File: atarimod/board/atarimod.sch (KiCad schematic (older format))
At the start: 14 parts, among them IC1 74HC14D, IC2 74HC14D, IC3 74HC14D, IC4 74HC14D, P1 CONN_02X20, P2 CONN_02X10, U2 APE8865N-33-HF-3

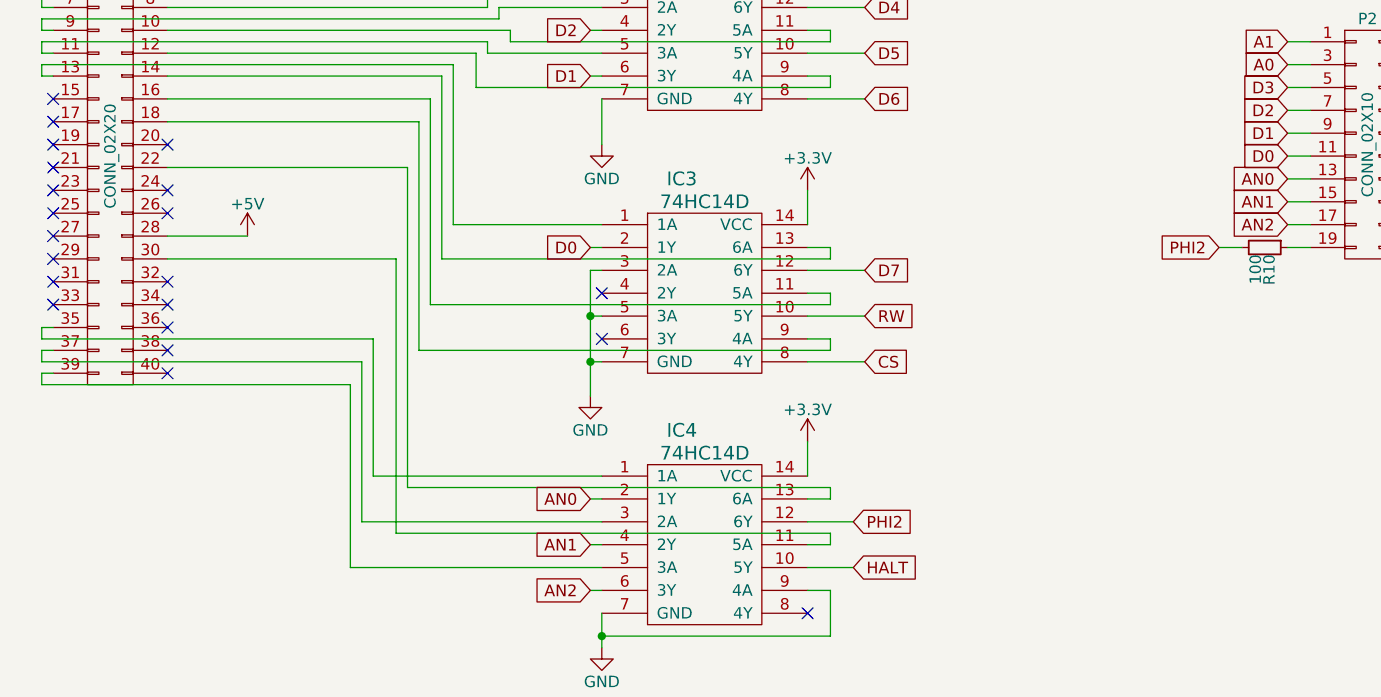
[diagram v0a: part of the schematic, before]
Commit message: Fixed a bug in the board layout
Working version now on Atari 800XL.
But in the mod board that needed some botching. Fixed in schematic and
layout. Removed buggy gerber files.
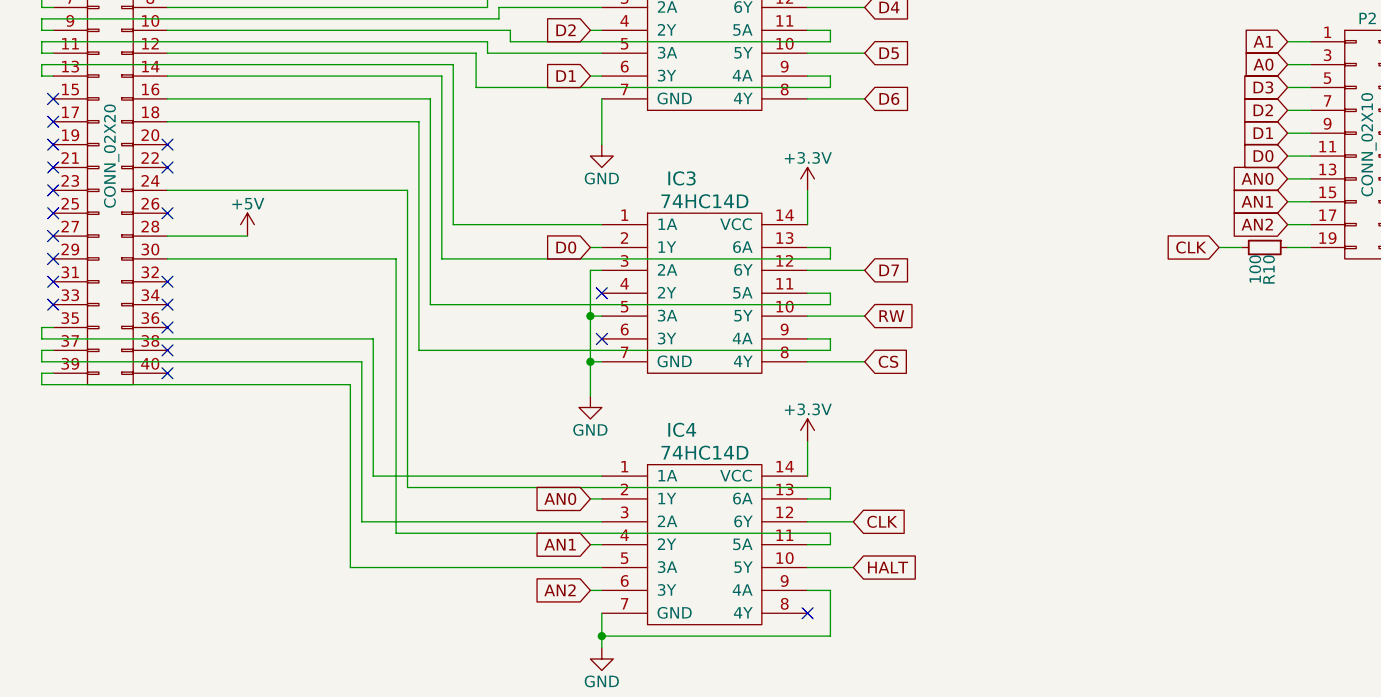
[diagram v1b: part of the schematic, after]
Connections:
- net at IC4.13 (6A): now also P1.24 (P24); no longer P1.22 (P22)
- net PHI2 renamed CLK
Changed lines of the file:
@@
 $EndDescr
 Text GLabel 7800 3400 0    51   Input ~ 0
-PHI2
+CLK
 Text GLabel 8800 3200 2    51   Input ~ 0
 RW
@@
 CS
 Text GLabel 6200 4600 2    51   Input ~ 0
-PHI2
+CLK
 Text GLabel 6200 4800 2    51   Input ~ 0
 HALT
@@
 $EndComp
 NoConn ~ 3200 3250
-NoConn ~ 3200 3150
 NoConn ~ 3200 2950
 Wire Wire Line
@@
 	4100 4400 5100 4400
 Wire Wire Line
-	3200 3050 4250 3050
-Wire Wire Line
 	4250 4450 6100 4450
 Wire Wire Line
@@
 	4200 3450 4200 4650
 Wire Wire Line
-	4250 3050 4250 4450
+	4250 3150 4250 4450
 Wire Wire Line
 	3200 2650 4400 2650
@@
 Wire Wire Line
 	8700 2500 8800 2500
+Wire Wire Line
+	3200 3150 4250 3150
+NoConn ~ 3200 3050
 $EndSCHEMATC

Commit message: Revision 3 of Atari GTIA Adapter
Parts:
- removed P1: CONN_02X20, Pin_Headers:Pin_Header_Straight_2x20_Pitch2.54mm, symbol CONN_02X20
- added P1: DIP40_Socket, ProjectFootprints:socket_embedded_40pin, symbol Connector_Generic:Conn_02x20_Counter_Clockwise
- C1, C2: value 10uF -> 1uF; footprint Capacitors_SMD:C_0805_HandSoldering -> Capacitor_SMD:C_0805_2012Metric_Pad1.15x1.40mm_HandSolder; symbol C_Small -> Device:C_Small
- C3, C4, C5, C6: footprint Capacitors_SMD:C_0603_HandSoldering -> Capacitor_SMD:C_0603_1608Metric_Pad1.05x0.95mm_HandSolder; symbol C_Small -> Device:C_Small
- IC1, IC2, IC3, IC4: value 74HC14D -> SN74LVC14ADBR; footprint Housings_SOIC:SOIC-14_3.9x8.7mm_Pitch1.27mm -> Package_SO:SSOP-14_5.3x6.2mm_P0.65mm; symbol 74HC14D -> components:74HC14D
- P2: footprint Pin_Headers:Pin_Header_Angled_2x10_Pitch2.54mm -> Connector_PinHeader_2.54mm:PinHeader_2x10_P2.54mm_Vertical; symbol CONN_02X10 -> atarimod-rescue:CONN_02X10
- R10: footprint Resistors_SMD:R_0805_HandSoldering -> Resistor_SMD:R_0805_2012Metric_Pad1.15x1.40mm_HandSolder; symbol R_Small -> Device:R_Small
- U2: value APE8865N-33-HF-3 -> RT9166-33GVL; footprint TO_SOT_Packages_SMD:SOT-23 -> Package_TO_SOT_SMD:SOT-23; symbol APE8865N-33-HF-3 -> atarimod-rescue:APE8865N-33-HF-3
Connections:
- wire segments 180 -> 197
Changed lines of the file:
@@
-EESchema Schematic File Version 2
-LIBS:power
-LIBS:device
-LIBS:transistors
-LIBS:conn
-LIBS:linear
-LIBS:regul
-LIBS:74xx
-LIBS:cmos4000
-LIBS:adc-dac
-LIBS:memory
-LIBS:xilinx
-LIBS:microcontrollers
-LIBS:dsp
-LIBS:microchip
-LIBS:analog_switches
-LIBS:motorola
-LIBS:texas
-LIBS:intel
-LIBS:audio
-LIBS:interface
-LIBS:digital-audio
-LIBS:philips
-LIBS:display
-LIBS:cypress
-LIBS:siliconi
-LIBS:opto
-LIBS:atmel
-LIBS:contrib
-LIBS:valves
-LIBS:components
+EESchema Schematic File Version 4
 LIBS:atarimod-cache
-EELAYER 25 0
+EELAYER 26 0
 EELAYER END
 $Descr A4 11693 8268
 encoding utf-8
 Sheet 1 1
-Title "Atari mod board"
+Title "Atari GTIA adapter"
 Date ""
-Rev "2"
+Rev "3"
 Comp ""
 Comment1 ""
@@
 D4
 $Comp
-L 74HC14D IC1
+L components:74HC14D IC1
 U 1 1 59608C85
 P 5500 800
 F 0 "IC1" H 5450 850 60  0000 C CNN
-F 1 "74HC14D" H 5550 750 60  0000 C CNN
-F 2 "Housings_SOIC:SOIC-14_3.9x8.7mm_Pitch1.27mm" H 5550 800 60  0001 C CNN
+F 1 "SN74LVC14ADBR" H 5550 750 60  0000 C CNN
+F 2 "Package_SO:SSOP-14_5.3x6.2mm_P0.65mm" H 5550 800 60  0001 C CNN
 F 3 "" H 5550 800 60  0001 C CNN
 	1    5500 800
@@
 $EndComp
 $Comp
-L C_Small C4
+L Device:C_Small C4
 U 1 1 59609575
 P 2950 6850
 F 0 "C4" H 2960 6920 50  0000 L CNN
 F 1 "100nF" H 2960 6770 50  0000 L CNN
-F 2 "Capacitors_SMD:C_0603_HandSoldering" H 2950 6850 50  0001 C CNN
+F 2 "Capacitor_SMD:C_0603_1608Metric_Pad1.05x0.95mm_HandSolder" H 2950 6850 50  0001 C CNN
 F 3 "" H 2950 6850 50  0000 C CNN
 	1    2950 6850
@@
 $EndComp
 $Comp
-L 74HC14D IC2
+L components:74HC14D IC2
 U 1 1 59609BB1
 P 5500 2000
 F 0 "IC2" H 5450 2050 60  0000 C CNN
-F 1 "74HC14D" H 5550 1950 60  0000 C CNN
-F 2 "Housings_SOIC:SOIC-14_3.9x8.7mm_Pitch1.27mm" H 5550 2000 60  0001 C CNN
+F 1 "SN74LVC14ADBR" H 5550 1950 60  0000 C CNN
+F 2 "Package_SO:SSOP-14_5.3x6.2mm_P0.65mm" H 5550 2000 60  0001 C CNN
 F 3 "" H 5550 2000 60  0001 C CNN
 	1    5500 2000
@@
 $EndComp
 $Comp
-L C_Small C3
+L Device:C_Small C3
 U 1 1 59609BD6
 P 2600 6850
 F 0 "C3" H 2610 6920 50  0000 L CNN
 F 1 "100nF" H 2610 6770 50  0000 L CNN
-F 2 "Capacitors_SMD:C_0603_HandSoldering" H 2600 6850 50  0001 C CNN
+F 2 "Capacitor_SMD:C_0603_1608Metric_Pad1.05x0.95mm_HandSolder" H 2600 6850 50  0001 C CNN
 F 3 "" H 2600 6850 50  0000 C CNN
 	1    2600 6850
@@
 $EndComp
 $Comp
-L C_Small C6
+L Device:C_Small C6
 U 1 1 5960A791
 P 3650 6850
 F 0 "C6" H 3660 6920 50  0000 L CNN
 F 1 "100nF" H 3660 6770 50  0000 L CNN
-F 2 "Capacitors_SMD:C_0603_HandSoldering" H 3650 6850 50  0001 C CNN
+F 2 "Capacitor_SMD:C_0603_1608Metric_Pad1.05x0.95mm_HandSolder" H 3650 6850 50  0001 C CNN
 F 3 "" H 3650 6850 50  0000 C CNN
 	1    3650 6850
@@
 $EndComp
 $Comp
-L 74HC14D IC4
+L components:74HC14D IC4
 U 1 1 5960B79A
 P 5500 4250
 F 0 "IC4" H 5450 4300 60  0000 C CNN
-F 1 "74HC14D" H 5550 4200 60  0000 C CNN
-F 2 "Housings_SOIC:SOIC-14_3.9x8.7mm_Pitch1.27mm" H 5550 4250 60  0001 C CNN
+F 1 "SN74LVC14ADBR" H 5550 4200 60  0000 C CNN
+F 2 "Package_SO:SSOP-14_5.3x6.2mm_P0.65mm" H 5550 4250 60  0001 C CNN
 F 3 "" H 5550 4250 60  0001 C CNN
 	1    5500 4250
@@
 $EndComp
 $Comp
-L C_Small C5
+L Device:C_Small C5
 U 1 1 5960B7AE
 P 3300 6850
 F 0 "C5" H 3310 6920 50  0000 L CNN
 F 1 "100nF" H 3310 6770 50  0000 L CNN
-F 2 "Capacitors_SMD:C_0603_HandSoldering" H 3300 6850 50  0001 C CNN
+F 2 "Capacitor_SMD:C_0603_1608Metric_Pad1.05x0.95mm_HandSolder" H 3300 6850 50  0001 C CNN
 F 3 "" H 3300 6850 50  0000 C CNN
 	1    3300 6850
@@
 $EndComp
 $Comp
-L 74HC14D IC3
+L components:74HC14D IC3
 U 1 1 5960A76D
 P 5500 3150
 F 0 "IC3" H 5450 3200 60  0000 C CNN
-F 1 "74HC14D" H 5550 3100 60  0000 C CNN
-F 2 "Housings_SOIC:SOIC-14_3.9x8.7mm_Pitch1.27mm" H 5550 3150 60  0001 C CNN
+F 1 "SN74LVC14ADBR" H 5550 3100 60  0000 C CNN
+F 2 "Package_SO:SSOP-14_5.3x6.2mm_P0.65mm" H 5550 3150 60  0001 C CNN
 F 3 "" H 5550 3150 60  0001 C CNN
 	1    5500 3150
@@
 $EndComp
 $Comp
-L APE8865N-33-HF-3 U2
+L atarimod-rescue:APE8865N-33-HF-3 U2
 U 1 1 5960D9B8
 P 1700 6550
 F 0 "U2" H 1400 6800 50  0000 C CNN
-F 1 "APE8865N-33-HF-3" H 1700 6750 50  0000 C CNN
-F 2 "TO_SOT_Packages_SMD:SOT-23" H 1700 6650 50  0000 C CIN
+F 1 "RT9166-33GVL" H 1700 6750 50  0000 C CNN
+F 2 "Package_TO_SOT_SMD:SOT-23" H 1700 6650 50  0000 C CIN
 F 3 "" H 1700 6550 50  0000 C CNN
 	1    1700 6550
@@
 $EndComp
 $Comp
-L +3.3V #PWR01
+L power:+3.3V #PWR01
 U 1 1 5960DAF2
 P 2250 6500
@@
 $EndComp
 $Comp
-L GND #PWR02
+L power:GND #PWR02
 U 1 1 5960DB92
 P 1700 7250
@@
 $EndComp
 $Comp
-L C_Small C1
+L Device:C_Small C1
 U 1 1 5960DC33
 P 1100 6750
 F 0 "C1" H 1110 6820 50  0000 L CNN
-F 1 "10uF" H 1110 6670 50  0000 L CNN
-F 2 "Capacitors_SMD:C_0805_HandSoldering" H 1100 6750 50  0001 C CNN
+F 1 "1uF" H 1110 6670 50  0000 L CNN
+F 2 "Capacitor_SMD:C_0805_2012Metric_Pad1.15x1.40mm_HandSolder" H 1100 6750 50  0001 C CNN
 F 3 "" H 1100 6750 50  0000 C CNN
 	1    1100 6750
@@
 $EndComp
 $Comp
-L C_Small C2
+L Device:C_Small C2
 U 1 1 5960E580
 P 2200 6750
 F 0 "C2" H 2210 6820 50  0000 L CNN
-F 1 "10uF" H 2210 6670 50  0000 L CNN
-F 2 "Capacitors_SMD:C_0805_HandSoldering" H 2200 6750 50  0001 C CNN
+F 1 "1uF" H 2210 6670 50  0000 L CNN
+F 2 "Capacitor_SMD:C_0805_2012Metric_Pad1.15x1.40mm_HandSolder" H 2200 6750 50  0001 C CNN
 F 3 "" H 2200 6750 50  0000 C CNN
 	1    2200 6750
@@
 HALT
 $Comp
-L PWR_FLAG #FLG03
+L power:PWR_FLAG #FLG03
 U 1 1 596132DF
 P 1500 5950
@@
 $EndComp
 $Comp
-L PWR_FLAG #FLG04
+L power:PWR_FLAG #FLG04
 U 1 1 596135A4
 P 2050 7250
@@
 $EndComp
 $Comp
-L +5V #PWR05
+L power:+5V #PWR05
 U 1 1 5961413C
 P 1100 5950
@@
 $EndComp
 $Comp
-L CONN_02X10 P2
+L atarimod-rescue:CONN_02X10 P2
 U 1 1 5A2D6700
 P 8450 2950
 F 0 "P2" H 8450 3500 50  0000 C CNN
 F 1 "CONN_02X10" V 8450 2950 50  0000 C CNN
-F 2 "Pin_Headers:Pin_Header_Angled_2x10_Pitch2.54mm" H 8450 1750 50  0001 C CNN
+F 2 "Connector_PinHeader_2.54mm:PinHeader_2x10_P2.54mm_Vertical" H 8450 1750 50  0001 C CNN
 F 3 "" H 8450 1750 50  0000 C CNN
 	1    8450 2950
@@
 $EndComp
 $Comp
-L R_Small R10
+L Device:R_Small R10
 U 1 1 5A2D9629
 P 8000 3400
 F 0 "R10" H 8030 3420 50  0000 L CNN
 F 1 "100" H 8030 3360 50  0000 L CNN
-F 2 "Resistors_SMD:R_0805_HandSoldering" H 8000 3400 50  0001 C CNN
+F 2 "Resistor_SMD:R_0805_2012Metric_Pad1.15x1.40mm_HandSolder" H 8000 3400 50  0001 C CNN
 F 3 "" H 8000 3400 50  0000 C CNN
 	1    8000 3400
@@
 $EndComp
 $Comp
-L +3.3V #PWR06
+L power:+3.3V #PWR06
 U 1 1 5A30002C
 P 6000 750
@@
 $EndComp
 $Comp
-L +3.3V #PWR07
+L power:+3.3V #PWR07
 U 1 1 5A300104
 P 6000 1950
@@
 $EndComp
 $Comp
-L +3.3V #PWR08
+L power:+3.3V #PWR08
 U 1 1 5A300284
 P 6000 3150
@@
 $EndComp
 $Comp
-L +3.3V #PWR09
+L power:+3.3V #PWR09
 U 1 1 5A3003A2
 P 6000 4250
@@
 $EndComp
 $Comp
-L GND #PWR010
+L power:GND #PWR010
 U 1 1 5A300740
 P 5100 5150
@@
 $EndComp
 $Comp
-L GND #PWR011
+L power:GND #PWR011
 U 1 1 5A300834
 P 5050 4050
@@
 $EndComp
 $Comp
-L GND #PWR012
+L power:GND #PWR012
 U 1 1 5A3008C6
 P 5100 2950
@@
 $EndComp
 $Comp
-L GND #PWR013
+L power:GND #PWR013
 U 1 1 5A3009C8
 P 5050 1750
@@
 $EndComp
 $Comp
-L CONN_02X20 P1
-U 1 1 5A301E2A
-P 2950 3000
-F 0 "P1" H 2950 4050 50  0000 C CNN
-F 1 "CONN_02X20" V 2950 3000 50  0000 C CNN
-F 2 "Pin_Headers:Pin_Header_Straight_2x20_Pitch2.54mm" H 2950 2050 50  0001 C CNN
-F 3 "" H 2950 2050 50  0000 C CNN
-	1    2950 3000
-	1    0    0    -1
-$EndComp
-$Comp
-L GND #PWR014
+L power:GND #PWR014
 U 1 1 5A302918
 P 2300 2300
@@
 NoConn ~ 2700 2750
 $Comp
-L +5V #PWR015
+L power:+5V #PWR015
 U 1 1 5A303009
 P 3550 3350
@@
 NoConn ~ 3200 2950
 Wire Wire Line
-	2150 6500 2250 6500
+	2150 6500 2200 6500
 Wire Wire Line
 	2200 6650 2200 6500
@@
 Connection ~ 1100 6500
 Wire Wire Line
-	1700 6850 1700 7250
+	1700 6850 1700 7200
 Wire Wire Line
 	2050 7200 2050 7250
 Wire Wire Line
-	1100 7200 3650 7200
+	1100 7200 1700 7200
 Connection ~ 1700 7200
 Wire Wire Line
@@
 	1100 6850 1100 7200
 Wire Wire Line
-	1100 5950 1100 6650
+	1100 5950 1100 6100
 Wire Wire Line
 	1500 5950 1500 6100
@@
 Connection ~ 1100 6100
 Wire Wire Line
-	2200 6500 3650 6500
+	2200 6500 2600 6500
 Wire Wire Line
 	2600 6500 2600 6750
@@
 	5100 2750 5100 2950
 Wire Wire Line
-	5100 5000 5100 5150
+	5100 5000 5100 5100
 Wire Wire Line
 	6000 4400 6000 4250
@@
 	5100 1350 5050 1350
 Wire Wire Line
-	5050 1350 5050 1750
+	5050 1350 5050 1550
 Wire Wire Line
 	5100 1550 5050 1550
@@
 NoConn ~ 6000 5000
 Wire Wire Line
-	5050 3500 5050 4050
+	5050 3500 5050 3700
 Wire Wire Line
 	5050 3900 5100 3900
@@
 	3200 3150 4250 3150
 NoConn ~ 3200 3050
+Wire Wire Line
+	2200 6500 2250 6500
+Wire Wire Line
+	1100 6500 1100 6650
+Wire Wire Line
+	1700 7200 1700 7250
+Wire Wire Line
+	1700 7200 2050 7200
+Wire Wire Line
+	2050 7200 2200 7200
+Wire Wire Line
+	1100 6100 1100 6500
+Wire Wire Line
+	2600 6500 2950 6500
+Wire Wire Line
+	2950 6500 3300 6500
+Wire Wire Line
+	3300 6500 3650 6500
+Wire Wire Line
+	2200 7200 2600 7200
+Wire Wire Line
+	2600 7200 2950 7200
+Wire Wire Line
+	2950 7200 3300 7200
+Wire Wire Line
+	3300 7200 3650 7200
+Wire Wire Line
+	5050 1550 5050 1750
+Wire Wire Line
+	5050 3900 5050 4050
+Wire Wire Line
+	5050 3700 5050 3900
+Wire Wire Line
+	5100 5100 5100 5150
+$Comp
+L Connector_Generic:Conn_02x20_Counter_Clockwise P1
+U 1 1 5F17D2E6
+P 2900 2950
+F 0 "P1" H 2950 4067 50  0000 C CNN
+F 1 "DIP40_Socket" H 2950 3976 50  0000 C CNN
+F 2 "ProjectFootprints:socket_embedded_40pin" H 2900 2950 50  0001 C CNN
+F 3 "~" H 2900 2950 50  0001 C CNN
+	1    2900 2950
+	1    0    0    -1
+$EndComp
 $EndSCHEMATC

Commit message: Use different voltage regulator to reduce noise
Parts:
- removed U2: RT9166-33GVL, Package_TO_SOT_SMD:SOT-23, symbol atarimod-rescue:APE8865N-33-HF-3
- added U2: MIC5504-3.3YM5, Package_TO_SOT_SMD:SOT-23-5, symbol Regulator_Linear:MIC5504-3.3YM5
- C1, C2: value 1uF -> 10uF
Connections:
- wire segments 197 -> 200
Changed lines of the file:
@@
 Title "Atari GTIA adapter"
 Date ""
-Rev "3"
+Rev "4"
 Comp ""
 Comment1 ""
@@
 $EndComp
 $Comp
-L atarimod-rescue:APE8865N-33-HF-3 U2
-U 1 1 5960D9B8
-P 1700 6550
-F 0 "U2" H 1400 6800 50  0000 C CNN
-F 1 "RT9166-33GVL" H 1700 6750 50  0000 C CNN
-F 2 "Package_TO_SOT_SMD:SOT-23" H 1700 6650 50  0000 C CIN
-F 3 "" H 1700 6550 50  0000 C CNN
-	1    1700 6550
-	1    0    0    -1
-$EndComp
-$Comp
 L power:+3.3V #PWR01
 U 1 1 5960DAF2
@@
 P 1100 6750
 F 0 "C1" H 1110 6820 50  0000 L CNN
-F 1 "1uF" H 1110 6670 50  0000 L CNN
+F 1 "10uF" H 1110 6670 50  0000 L CNN
 F 2 "Capacitor_SMD:C_0805_2012Metric_Pad1.15x1.40mm_HandSolder" H 1100 6750 50  0001 C CNN
 F 3 "" H 1100 6750 50  0000 C CNN
@@
 P 2200 6750
 F 0 "C2" H 2210 6820 50  0000 L CNN
-F 1 "1uF" H 2210 6670 50  0000 L CNN
+F 1 "10uF" H 2210 6670 50  0000 L CNN
 F 2 "Capacitor_SMD:C_0805_2012Metric_Pad1.15x1.40mm_HandSolder" H 2200 6750 50  0001 C CNN
 F 3 "" H 2200 6750 50  0000 C CNN
@@
 NoConn ~ 3200 2950
 Wire Wire Line
-	2150 6500 2200 6500
-Wire Wire Line
 	2200 6650 2200 6500
 Connection ~ 2200 6500
@@
 	1100 6500 1250 6500
 Connection ~ 1100 6500
-Wire Wire Line
-	1700 6850 1700 7200
 Wire Wire Line
 	2050 7200 2050 7250
@@
 	1    0    0    -1
 $EndComp
+$Comp
+L Regulator_Linear:MIC5504-3.3YM5 U2
+U 1 1 5F623D94
+P 1700 6600
+F 0 "U2" H 1700 6967 50  0000 C CNN
+F 1 "MIC5504-3.3YM5" H 1700 6876 50  0000 C CNN
+F 2 "Package_TO_SOT_SMD:SOT-23-5" H 1700 6200 50  0001 C CNN
+F 3 "http://ww1.microchip.com/downloads/en/DeviceDoc/MIC550X.pdf" H 1450 6850 50  0001 C CNN
+	1    1700 6600
+	1    0    0    -1
+$EndComp
+Wire Wire Line
+	1250 6500 1250 6700
+Wire Wire Line
+	1250 6700 1300 6700
+Wire Wire Line
+	1250 6500 1300 6500
+Connection ~ 1250 6500
+Wire Wire Line
+	2100 6500 2200 6500
+Wire Wire Line
+	1700 7200 1700 6900
 $EndSCHEMATC
